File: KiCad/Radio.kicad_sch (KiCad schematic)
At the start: 2 parts, among them J1 CON-SMA-EDGE-S, U1 RFM95W-868S2

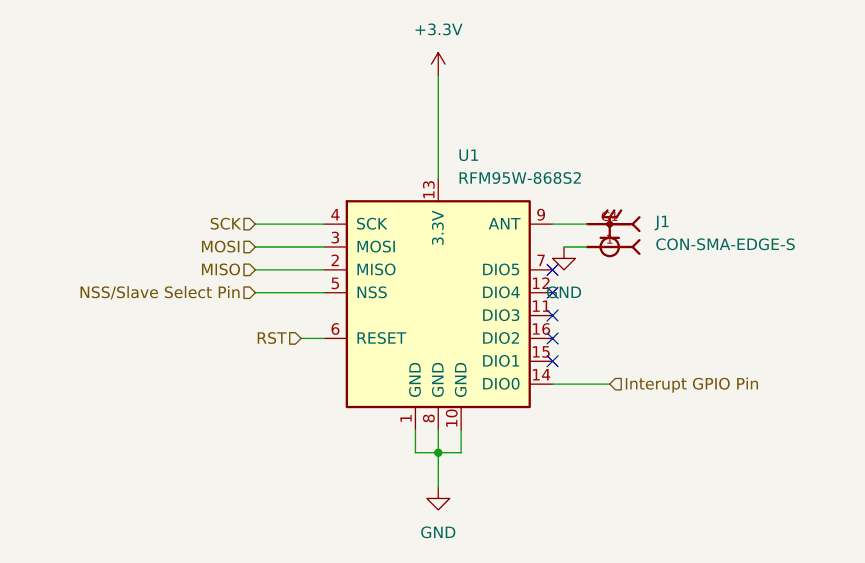
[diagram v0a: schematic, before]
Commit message: Reset all annotationss
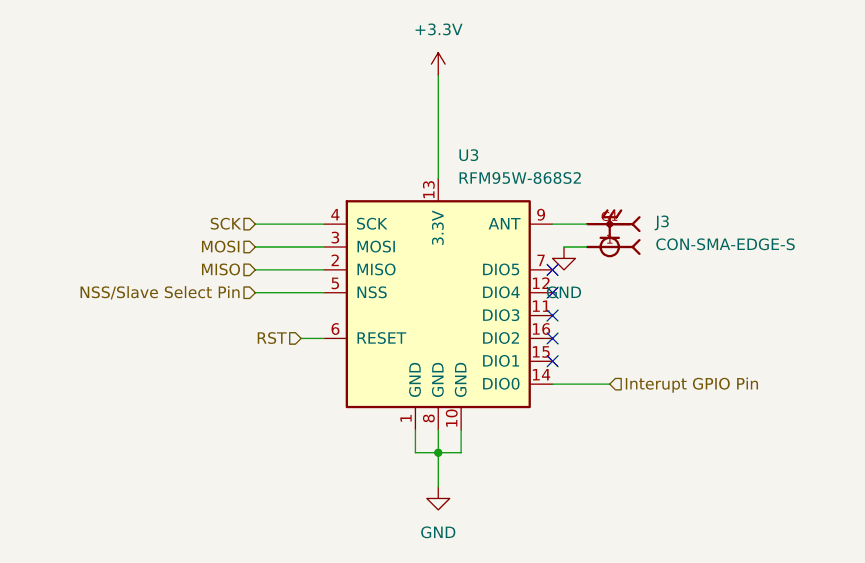
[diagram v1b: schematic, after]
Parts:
- renumbered J1 to J3, U1 to U3
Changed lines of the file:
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@@
 		(dnp no)
 		(fields_autoplaced yes)
-		(property "Reference" "#PWR02"
+		(property "Reference" "#PWR043"
 			(at 147.32 92.71 0)
 			(effects
@@
 			(project ""
 				(path "/16f8cce7-467e-4342-b55a-00af81cd6f69/1c8bf498-9754-4bec-a707-8e930cfc3fe5"
-					(reference "#PWR02")
+					(reference "#PWR043")
 					(unit 1)
 				)
@@
 		(on_board yes)
 		(dnp no)
-		(property "Reference" "U1"
+		(property "Reference" "U3"
 			(at 135.5441 76.2 0)
 			(effects
@@
 			(project ""
 				(path "/16f8cce7-467e-4342-b55a-00af81cd6f69/1c8bf498-9754-4bec-a707-8e930cfc3fe5"
-					(reference "U1")
+					(reference "U3")
 					(unit 1)
 				)
@@
 		(dnp no)
 		(fields_autoplaced yes)
-		(property "Reference" "#PWR01"
+		(property "Reference" "#PWR041"
 			(at 133.35 71.12 0)
 			(effects
@@
 			(project ""
 				(path "/16f8cce7-467e-4342-b55a-00af81cd6f69/1c8bf498-9754-4bec-a707-8e930cfc3fe5"
-					(reference "#PWR01")
+					(reference "#PWR041")
 					(unit 1)
 				)
@@
 		(dnp no)
 		(fields_autoplaced yes)
-		(property "Reference" "#PWR03"
+		(property "Reference" "#PWR042"
 			(at 133.35 119.38 0)
 			(effects
@@
 			(project ""
 				(path "/16f8cce7-467e-4342-b55a-00af81cd6f69/1c8bf498-9754-4bec-a707-8e930cfc3fe5"
-					(reference "#PWR03")
+					(reference "#PWR042")
 					(unit 1)
 				)
@@
 		(dnp no)
 		(fields_autoplaced yes)
-		(property "Reference" "J1"
+		(property "Reference" "J3"
 			(at 157.48 83.5659 0)
 			(effects
@@
 			(project ""
 				(path "/16f8cce7-467e-4342-b55a-00af81cd6f69/1c8bf498-9754-4bec-a707-8e930cfc3fe5"
-					(reference "J1")
-					(unit 1)
-				)
+					(reference "J3")
+					(unit 1)
+				)

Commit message: Updated several footprints
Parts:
- U3: footprint (none) -> RF_Module:HOPERF_RFM9XW_SMD
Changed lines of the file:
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@@
 			)
 		)
-		(property "Footprint" ""
+		(property "Footprint" "RF_Module:HOPERF_RFM9XW_SMD"
 			(at 49.53 49.53 0)
 			(effects

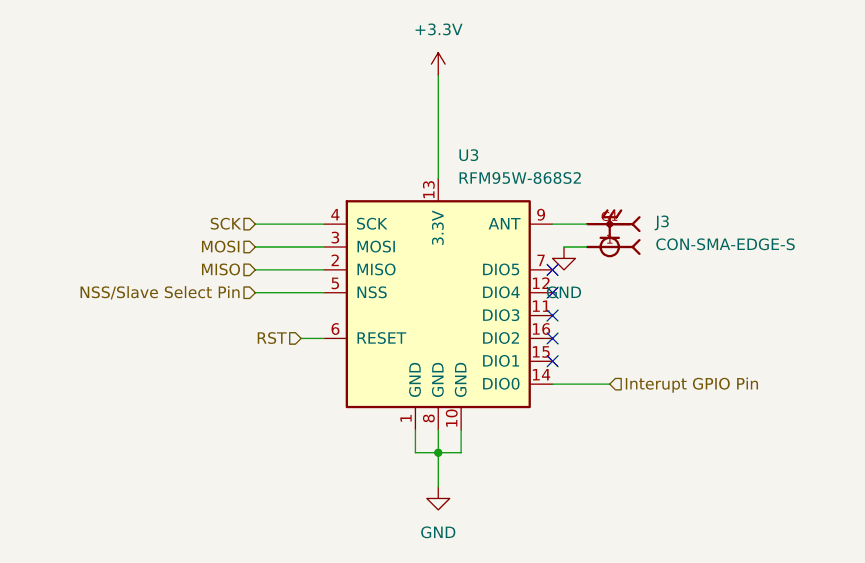
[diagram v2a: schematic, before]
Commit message: Added Pyrochannels
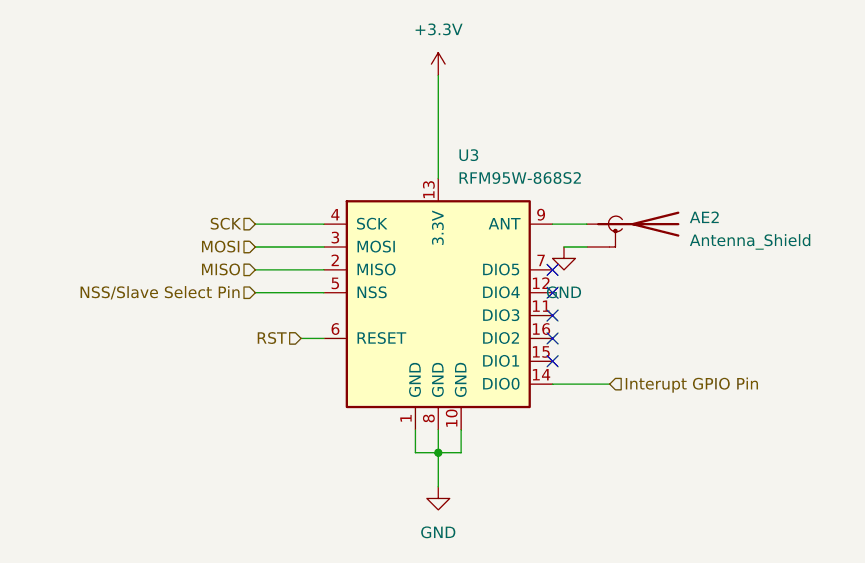
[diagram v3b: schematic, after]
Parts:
- removed J3: CON-SMA-EDGE-S, CON-SMA-EDGE-S:RFSOLUTIONS_CON-SMA-EDGE-S, symbol CON-SMA-EDGE-S:CON-SMA-EDGE-S
- added AE2: Antenna_Shield, CON-SMA-EDGE-S:RFSOLUTIONS_CON-SMA-EDGE-S, symbol Device:Antenna_Shield
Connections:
- net GND: now also AE2.2 (Shield)
- net at U3.9 (ANT): now also AE2.1 (A)
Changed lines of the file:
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@@
+	)
+	(symbol
+		(lib_id "Device:Antenna_Shield")
+		(at 154.94 83.82 270)
+		(unit 1)
+		(exclude_from_sim no)
+		(in_bom yes)
+		(on_board yes)
+		(dnp no)
+		(fields_autoplaced yes)
+		(property "Reference" "AE2"
+			(at 161.29 83.1214 90)
+			(effects
+				(font
+					(size 1.27 1.27)
+				)
+				(justify left)
+			)
+		)
+		(property "Value" "Antenna_Shield"
+			(at 161.29 85.6614 90)
+			(effects
+				(font
+					(size 1.27 1.27)
+				)
+				(justify left)
+			)
+		)
+		(property "Footprint" "CON-SMA-EDGE-S:RFSOLUTIONS_CON-SMA-EDGE-S"
+			(at 157.48 83.82 0)
+			(effects
+				(font
+					(size 1.27 1.27)
+				)
+				(hide yes)
+			)
+		)
+		(property "Datasheet" "~"
+			(at 157.48 83.82 0)
+			(effects
+				(font
+					(size 1.27 1.27)
+				)
+				(hide yes)
+			)
+		)
+		(property "Description" "Antenna with extra pin for shielding"
+			(at 154.94 83.82 0)
+			(effects
+				(font
+					(size 1.27 1.27)
+				)
+				(hide yes)
+			)
+		)
+		(pin "2"
+		)
+		(pin "1"
+		)
+		(instances
+			(project ""
+				(path "/16f8cce7-467e-4342-b55a-00af81cd6f69/1c8bf498-9754-4bec-a707-8e930cfc3fe5"
+					(reference "AE2")
+					(unit 1)
+				)
+			)
+		)
 	)
 	(symbol
@@
 					(unit 1)
 				)
-			)
-		)
-	)
-	(symbol
-		(lib_id "CON-SMA-EDGE-S:CON-SMA-EDGE-S")
-		(at 152.4 83.82 180)
-		(unit 1)
-		(exclude_from_sim no)
-		(in_bom yes)
-		(on_board yes)
-		(dnp no)
-		(fields_autoplaced yes)
-		(property "Reference" "J3"
-			(at 157.48 83.5659 0)
-			(effects
-				(font
-					(size 1.27 1.27)
-				)
-				(justify right)
-			)
-		)
-		(property "Value" "CON-SMA-EDGE-S"
-			(at 157.48 86.1059 0)
-			(effects
-				(font
-					(size 1.27 1.27)
-				)
-				(justify right)
-			)
-		)
-		(property "Footprint" "CON-SMA-EDGE-S:RFSOLUTIONS_CON-SMA-EDGE-S"
-			(at 152.4 83.82 0)
-			(effects
-				(font
-					(size 1.27 1.27)
-				)
-				(justify bottom)
-				(hide yes)
-			)
-		)
-		(property "Datasheet" ""
-			(at 152.4 83.82 0)
-			(effects
-				(font
-					(size 1.27 1.27)
-				)
-				(hide yes)
-			)
-		)
-		(property "Description" ""
-			(at 152.4 83.82 0)
-			(effects
-				(font
-					(size 1.27 1.27)
-				)
-				(hide yes)
-			)
-		)
-		(property "PARTREV" "1"
-			(at 152.4 83.82 0)
-			(effects
-				(font
-					(size 1.27 1.27)
-				)
-				(justify bottom)
-				(hide yes)
-			)
-		)
-		(property "STANDARD" "Manufacturer Recommendations"
-			(at 152.4 83.82 0)
-			(effects
-				(font
-					(size 1.27 1.27)
-				)
-				(justify bottom)
-				(hide yes)
-			)
-		)
-		(property "MAXIMUM_PACKAGE_HEIGHT" "6.35mm"
-			(at 152.4 83.82 0)
-			(effects
-				(font
-					(size 1.27 1.27)
-				)
-				(justify bottom)
-				(hide yes)
-			)
-		)
-		(property "MANUFACTURER" "RF Solutions"
-			(at 152.4 83.82 0)
-			(effects
-				(font
-					(size 1.27 1.27)
-				)
-				(justify bottom)
-				(hide yes)
-			)
-		)
-		(pin "G1"
-		)
-		(pin "1"
-		)
-		(instances
-			(project ""
-				(path "/16f8cce7-467e-4342-b55a-00af81cd6f69/1c8bf498-9754-4bec-a707-8e930cfc3fe5"
-					(reference "J3")
-					(unit 1)
-				)
-			)
-			(project ""
-				(path "/760e4be0-0457-4cde-a6ec-d56d0abadbc7"
-					(reference "J1")
-					(unit 1)
-				)

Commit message: Layout started
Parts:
- AE2: footprint CON-SMA-EDGE-S:RFSOLUTIONS_CON-SMA-EDGE-S -> Connector_Coaxial:SMA_Samtec_SMA-J-P-H-ST-EM1_EdgeMount
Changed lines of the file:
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@@
 			)
 		)
-		(property "Footprint" "CON-SMA-EDGE-S:RFSOLUTIONS_CON-SMA-EDGE-S"
+		(property "Footprint" "Connector_Coaxial:SMA_Samtec_SMA-J-P-H-ST-EM1_EdgeMount"
 			(at 157.48 83.82 0)
 			(effects

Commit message: Layout updated. Very little left to do.
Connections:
- net +3.3V renamed +3V3
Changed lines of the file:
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@@
 	)
 	(symbol
-		(lib_id "power:+3.3V")
+		(lib_id "power:+3V3")
 		(at 133.35 67.31 0)
 		(unit 1)
@@
 		(dnp no)
 		(fields_autoplaced yes)
-		(property "Reference" "#PWR041"
+		(property "Reference" "#PWR038"
 			(at 133.35 71.12 0)
 			(effects
@@
 			)
 		)
-		(property "Value" "+3.3V"
+		(property "Value" "+3V3"
 			(at 133.35 62.23 0)
 			(effects
@@
 			)
 		)
-		(property "Description" "Power symbol creates a global label with name \"+3.3V\""
+		(property "Description" "Power symbol creates a global label with name \"+3V3\""
 			(at 133.35 67.31 0)
 			(effects
@@
 			(project ""
 				(path "/16f8cce7-467e-4342-b55a-00af81cd6f69/1c8bf498-9754-4bec-a707-8e930cfc3fe5"
-					(reference "#PWR041")
+					(reference "#PWR038")
 					(unit 1)
 				)
-			)
-			(project ""
-				(path "/760e4be0-0457-4cde-a6ec-d56d0abadbc7"
-					(reference "#PWR01")
-					(unit 1)
-				)
